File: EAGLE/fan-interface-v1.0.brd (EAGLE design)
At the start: 25.4 x 25.4 mm, 27 parts, among them J2 QWIIC_RIGHT_ANGLE, U1 SN74LVC2G14DBVT, U2 SN74LVC2G14DBVT

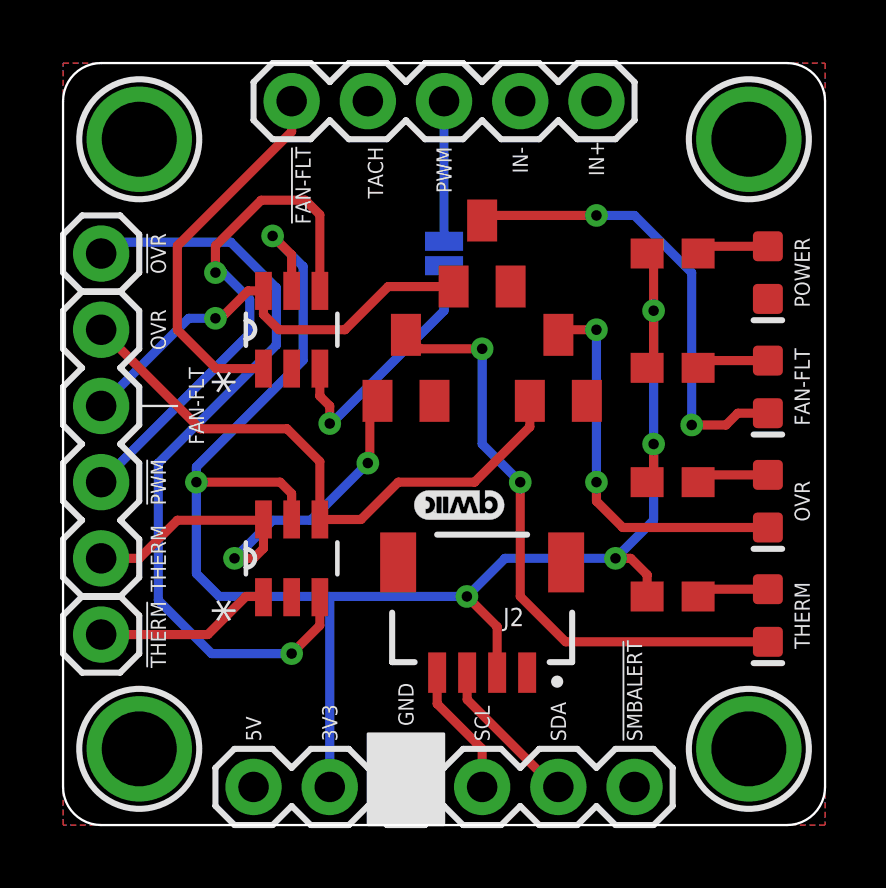
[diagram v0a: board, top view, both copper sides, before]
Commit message: added active buzzer
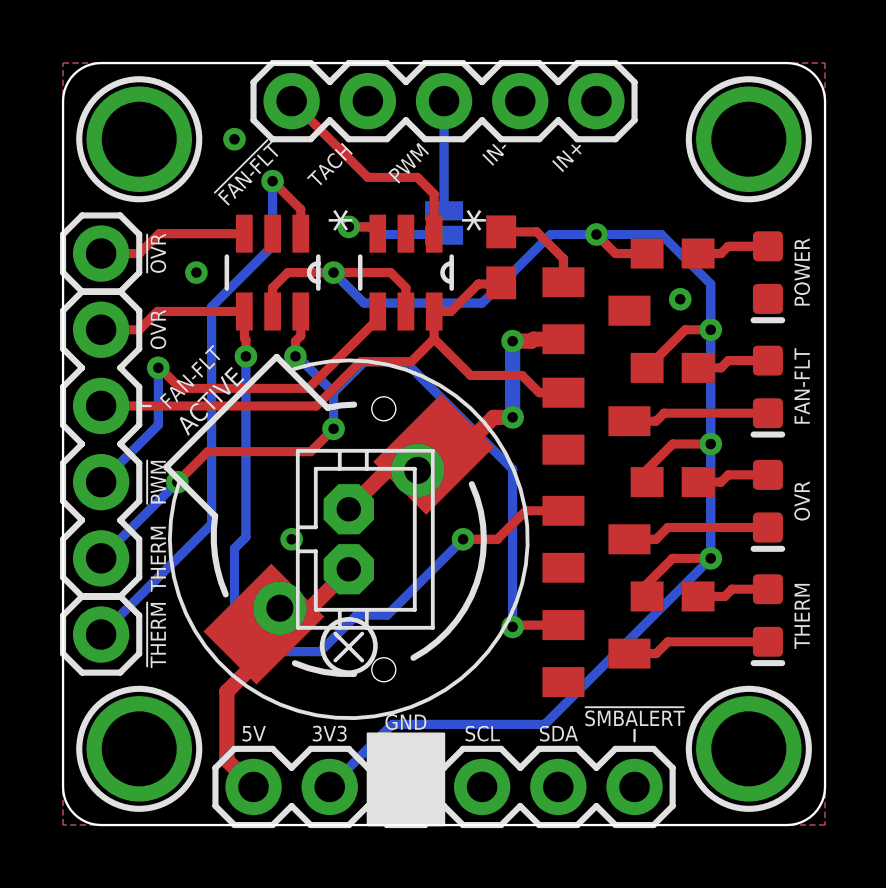
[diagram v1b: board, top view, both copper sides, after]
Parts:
- removed J6: (no value), SparkFun-Connectors:1X01
- removed LOGO2: QWIIC_LOGO_3MM, SparkFun-Aesthetics:QWIIC_3MM
- added ACTIVE: BUZZER, VinoRodrigues_Custom_Eagle:BUZZER-SMD
- added Q4: S8550, semicon-smd-ipc:SOT23
- added R5: 1k, SparkFun-Resistors:0603
- added U$2: JST-PH-2, VinoRodrigues_Custom_Eagle:JST-PH2
- J1: device SparkFun-Connectors:1X04 -> SparkFun-Connectors:1X05
- J2: value QWIIC_RIGHT_ANGLE -> (none); device SparkFun-Connectors:JST04_1MM_RA -> SparkFun-Connectors:1X06
- J3: device SparkFun-Connectors:1X05 -> SparkFun-Connectors:1X04
- J4: device SparkFun-Connectors:1X06 -> SparkFun-Connectors:1X01
- moved J4 18.5 mm to (1.27, 19.1)
- moved J1 18.2 mm to (17.8, 24.1), turned to 180 degrees
- moved J3 18.2 mm to (1.27, 16.5), turned to 270 degrees
- moved J5 12.7 mm to (1.27, 6.35)
- moved Q1 11.4 mm to (17.8, 5.71), turned to 270 degrees
- moved U1 9.55 mm to (6.99, 18.4), turned to 270 degrees
- moved J2 8.52 mm to (6.35, 1.27), turned to 0 degrees
- moved Q3 6.76 mm to (17.8, 13.5), turned to 270 degrees
- moved LOGO1 6.29 mm to (19.8, 14.6)
- moved Q2 5.85 mm to (17.8, 9.53), turned to 270 degrees
- moved U$1 5.61 mm to (19.8, 10.5)
- moved U2 4.26 mm to (11.4, 18.4), turned to 270 degrees
- moved PWM 1.02 mm to (12.7, 20.1)
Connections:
- new net N$11: ACTIVE.-, ACTIVE.-1, Q4.2, U$2.2
- new net N$7: Q4.1, R5.1
- net !FAN-FAULT: now also J1.5; no longer J3.5
- net !OVR: now also J4.1; no longer J5.1
- net !PWM: now also J3.3; no longer J1.3
- net !SMBALERT: now also J2.6; no longer J4.6
- net !THERM: now also J5.1; no longer J6.1
- net 3.3V: no longer J4.2
- net 5V: now also ACTIVE.+, ACTIVE.+1, J2.1, U$2.1; no longer J4.1
- net FAN-FAULT: now also J3.2, R5.2; no longer J1.2
- net GND: now also J2.3, Q4.3; no longer J2.1, J4.3
- net IN+: now also J1.1; no longer J3.1
- net IN-: now also J1.2; no longer J3.2
- net OVR: now also J3.1; no longer J1.1
- net PWM: now also J1.3; no longer J3.3
- net SCL: no longer J4.4
- net SDA: now also J2.5; no longer J2.3, J4.5
- net TACH: now also J1.4; no longer J3.4
- net THERM: now also J3.4; no longer J1.4
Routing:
- net !OVR: track 26.1 -> 5.05 mm, vias 1 -> 0
- net N$2: track 20.4 -> 4.78 mm, vias 2 -> 0
- net !THERM: track 5.95 -> 19.6 mm, vias 0 -> 1
- net THERM: track 16.0 -> 28.9 mm, vias 2 -> 4
- net N$11: track 0.00 -> 11.0 mm, vias 0 -> 2
- net N$9: track 15.6 -> 4.73 mm, vias 2 -> 0
- net 5V: track 0.00 -> 9.90 mm
- net OVR: track 20.2 -> 29.0 mm, vias 0 -> 2
- net N$5: track 13.2 -> 4.78 mm, vias 2 -> 0
- net FAN-FAULT: track 14.9 -> 20.6 mm, vias 1 -> 0
- net !FAN-FAULT: track 12.6 -> 7.35 mm
- net SDA: track 5.14 -> 0.00 mm
- net N$6: track 8.84 -> 4.35 mm
- net SCL: track 4.43 -> 0.00 mm
- net !PWM: track 17.4 -> 13.4 mm
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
